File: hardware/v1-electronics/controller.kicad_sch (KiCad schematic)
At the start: 35 parts, among them IC1 IS31FL3733-QFLS4-TR, IC2 IS31FL3733-QFLS4-TR, J2 Conn_01x03, U1 MDBT50Q-1MV2

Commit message: refactor(v1 hardware): power system
Beefed up power system.
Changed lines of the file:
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@@
 		)
 		(fill
-			(type none)
+			(type color)
+			(color 255 229 191 1)
 		)
 	)
@@
 	(rectangle
 		(start 317.5 149.86)
-		(end 381 177.8)
+		(end 368.3 177.8)
 		(stroke
 			(width 0.2)
@@
 	(text "Unassigned Pins"
 		(exclude_from_sim no)
-		(at 370.84 152.4 0)
+		(at 358.14 152.4 0)
 		(effects
 			(font
@@
 		)
 	)
+	(global_label "TPS61288_EN"
+		(shape input)
+		(at 345.44 170.18 0)
+		(fields_autoplaced yes)
+		(effects
+			(font
+				(size 1.27 1.27)
+			)
+			(justify left)
+		)
+		(property "Intersheetrefs" "${INTERSHEET_REFS}"
+			(at 361.3669 170.18 0)
+			(hide yes)
+			(show_name no)
+			(do_not_autoplace no)
+			(effects
+				(font
+					(size 1.27 1.27)
+				)
+				(justify left)
+			)
+		)
+	)
 	(global_label "CS4_2"
 		(shape input)
@@
 	(global_label "BQ25186_INT"
 		(shape input)
-		(at 350.52 160.02 0)
+		(at 345.44 160.02 0)
 		(fields_autoplaced yes)
 		(effects
@@
 		)
 		(property "Intersheetrefs" "${INTERSHEET_REFS}"
-			(at 366.0237 160.02 0)
+			(at 360.9437 160.02 0)
 			(hide yes)
 			(show_name no)
@@
 	(global_label "IS31FL3733_INTB2"
 		(shape input)
-		(at 345.44 165.1 180)
+		(at 340.36 167.64 180)
 		(fields_autoplaced yes)
 		(effects
@@
 		)
 		(property "Intersheetrefs" "${INTERSHEET_REFS}"
-			(at 337.0724 165.1 0)
+			(at 331.9924 167.64 0)
 			(hide yes)
 			(show_name no)
@@
 	(global_label "BQ25186_PG{slash}GPO"
 		(shape input)
-		(at 350.52 162.56 0)
+		(at 345.44 162.56 0)
 		(fields_autoplaced yes)
 		(effects
@@
 		)
 		(property "Intersheetrefs" "${INTERSHEET_REFS}"
-			(at 370.8618 162.56 0)
+			(at 365.7818 162.56 0)
 			(hide yes)
 			(show_name no)
@@
 		)
 	)
+	(global_label "~{MP2721_INT}"
+		(shape input)
+		(at 345.44 172.72 0)
+		(fields_autoplaced yes)
+		(effects
+			(font
+				(size 1.27 1.27)
+			)
+			(justify left)
+		)
+		(property "Intersheetrefs" "${INTERSHEET_REFS}"
+			(at 359.8551 172.72 0)
+			(hide yes)
+			(show_name no)
+			(do_not_autoplace no)
+			(effects
+				(font
+					(size 1.27 1.27)
+				)
+				(justify left)
+			)
+		)
+	)
 	(global_label "RE10_B-Channel"
 		(shape input)
@@
 	(global_label "BQ25186_CE"
 		(shape input)
-		(at 350.52 165.1 0)
+		(at 345.44 165.1 0)
 		(fields_autoplaced yes)
 		(effects
@@
 		)
 		(property "Intersheetrefs" "${INTERSHEET_REFS}"
-			(at 365.5398 165.1 0)
+			(at 360.4598 165.1 0)
 			(hide yes)
 			(show_name no)
@@
 	(global_label "IS31FL3733_INTB1"
 		(shape input)
-		(at 345.44 162.56 180)
+		(at 340.36 165.1 180)
 		(fields_autoplaced yes)
 		(effects
@@
 		)
 		(property "Intersheetrefs" "${INTERSHEET_REFS}"
-			(at 337.0724 162.56 0)
+			(at 331.9924 165.1 0)
 			(hide yes)
 			(show_name no)
@@
 	(global_label "IS31FL3733_SDB2"
 		(shape input)
-		(at 345.44 160.02 180)
+		(at 340.36 162.56 180)
 		(fields_autoplaced yes)
 		(effects
@@
 		)
 		(property "Intersheetrefs" "${INTERSHEET_REFS}"
-			(at 337.4958 160.02 0)
+			(at 332.4158 162.56 0)
 			(hide yes)
 			(show_name no)
@@
 	(global_label "IS31FL3733_SDB1"
 		(shape input)
-		(at 345.44 157.48 180)
+		(at 340.36 160.02 180)
 		(fields_autoplaced yes)
 		(effects
@@
 		)
 		(property "Intersheetrefs" "${INTERSHEET_REFS}"
-			(at 337.4958 157.48 0)
+			(at 332.4158 160.02 0)
 			(hide yes)
 			(show_name no)

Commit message: refactor(v1 hardware): power system refactor complete
- changed components and cleaned up schematic
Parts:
- removed C40: C_Small_US, symbol Device:C_Small_US
- removed C46: C_Small, symbol Device:C_Small
- removed R117, R118: R_Small, symbol Device:R_Small
- added C28: C_Small_US, symbol Device:C_Small_US
- added C40: C_Small, symbol Device:C_Small
- added R104, R105: R_Small, symbol Device:R_Small
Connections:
- net GND: now also C21.2, C23.2, C24.1, R103.1, R113.1, R114.1, R115.1, R116.1, C28.2, C40.1, R105.1; no longer C21.1, C23.1, C24.2, IC1.12 (PGND_2), IC1.5 (PGND_1), IC2.12 (PGND_2), IC2.5 (PGND_1), R103.2, R113.2, R114.2, R116.2
- net IICRST1: now also R113.2; no longer R113.1
- net IICRST2: now also R115.2
- net IS31FL3733_INTB2: now also R104.2; no longer R115.2
- net IS31FL3733_SDB1: now also R103.2; no longer R103.1
- net IS31FL3733_SDB2: now also R105.2; no longer R116.1
- net R_EXT1: now also R114.2; no longer R114.1
- net R_EXT2: now also R116.2
- net VDD: now also C24.2, R104.1; no longer C24.1, R115.1
- net V_SYS: now also C23.1, C28.1, C40.2; no longer C23.2
- net V_RAW_USB renamed VBUS
- net VBUS: now also C21.1; no longer C21.2
- new net Earth: IC1.12 (PGND_2), IC1.5 (PGND_1), IC2.12 (PGND_2), IC2.5 (PGND_1)
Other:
- note added: "High Current Noise Reduction"
- note added: "Not sure about decoupling these"
- note added: "We have 5 open pins. And 6 signals. We could combine interrupts. 4 signals then. and the enables into a single"
- note removed: "I'm uncertain about how to (if at all) decouple the VDD line"
- note removed: "Optional"
- moved on the sheet: C21, C22, C23, C25, C33, C35, C36, C37, C38, C39, J2, R102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

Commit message: feat(v1 hardware): select passives values
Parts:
- removed R43, R44: R_Small, symbol Device:R_Small
- added JP1: Jumper_2_Open, symbol Jumper:Jumper_2_Open
- added SW78: SW_Push, symbol Switch:SW_Push
- C21, C22, C23: value C_Small -> 10μF
- C24, C26, C33, C35, C36, C40, C41, C42: value C_Small -> 0.47μF
- C25, C28: value C_Small_US -> 22μF
- C37, C38, C39, C43, C44, C45: value C_Small -> 0.1μF
- R102, R103, R104, R105, R113, R115: value R_Small -> 100kΩ
- R114, R116: value R_Small -> 13kΩ
- R41, R42: value R_Small -> 10kΩ
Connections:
- net GND: now also SW78.1
- net RESET: now also SW78.2
- net SWDCLK: now also J2.1 (Pin_1)
- net SWDIO: now also J2.3 (Pin_3)
- net SYNC renamed SYNC1
- net SYNC1: now also JP1.1 (A); no longer IC2.40 (SYNC)
- new net SYNC2: IC2.40 (SYNC), JP1.2 (B)
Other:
- note added: "Mention USB here some where"
- note added: "The output current of each current soucecis set to 64mA. Each LED should see about 5mA at max current setting."
- note added: "pick theses based on the capacitance of the line"
- note removed: "USB Config"
- moved on the sheet: J2

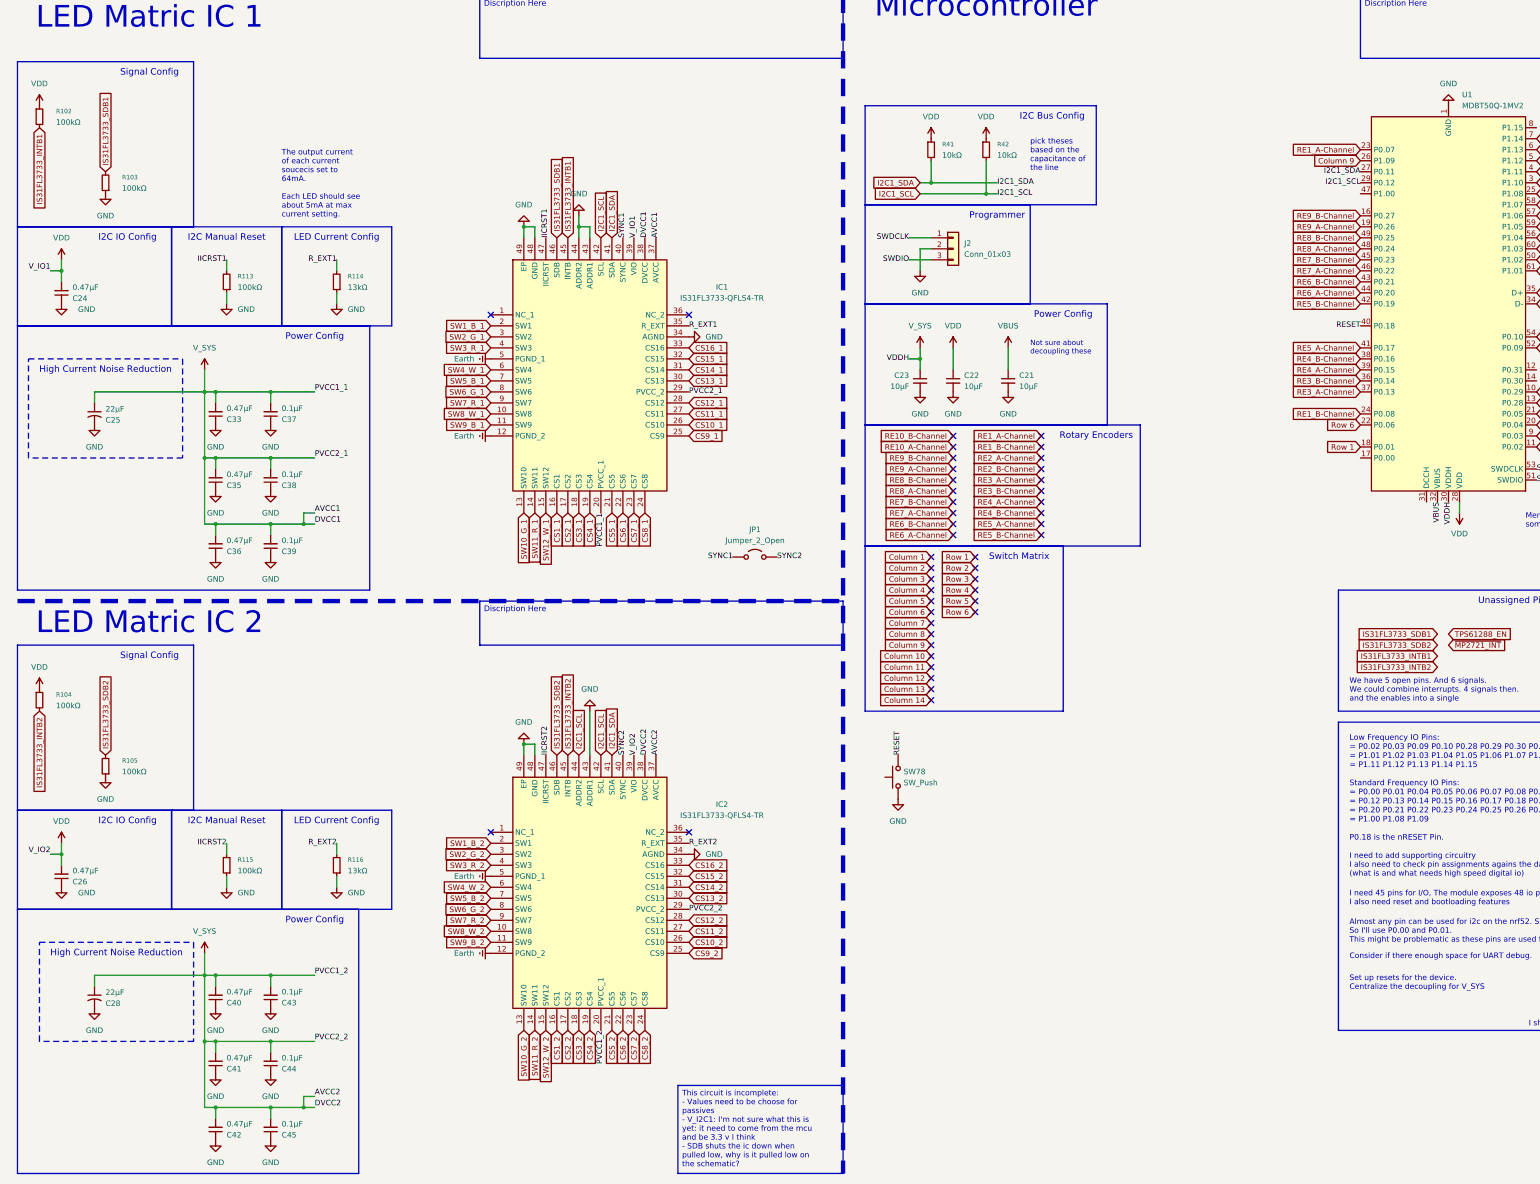
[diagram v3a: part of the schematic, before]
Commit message: refactor(v1 hardware): convert switch matrix to hierarchical pins
made other changes
had claude generate a script for making the convertion
the references for this file still need to be fixed
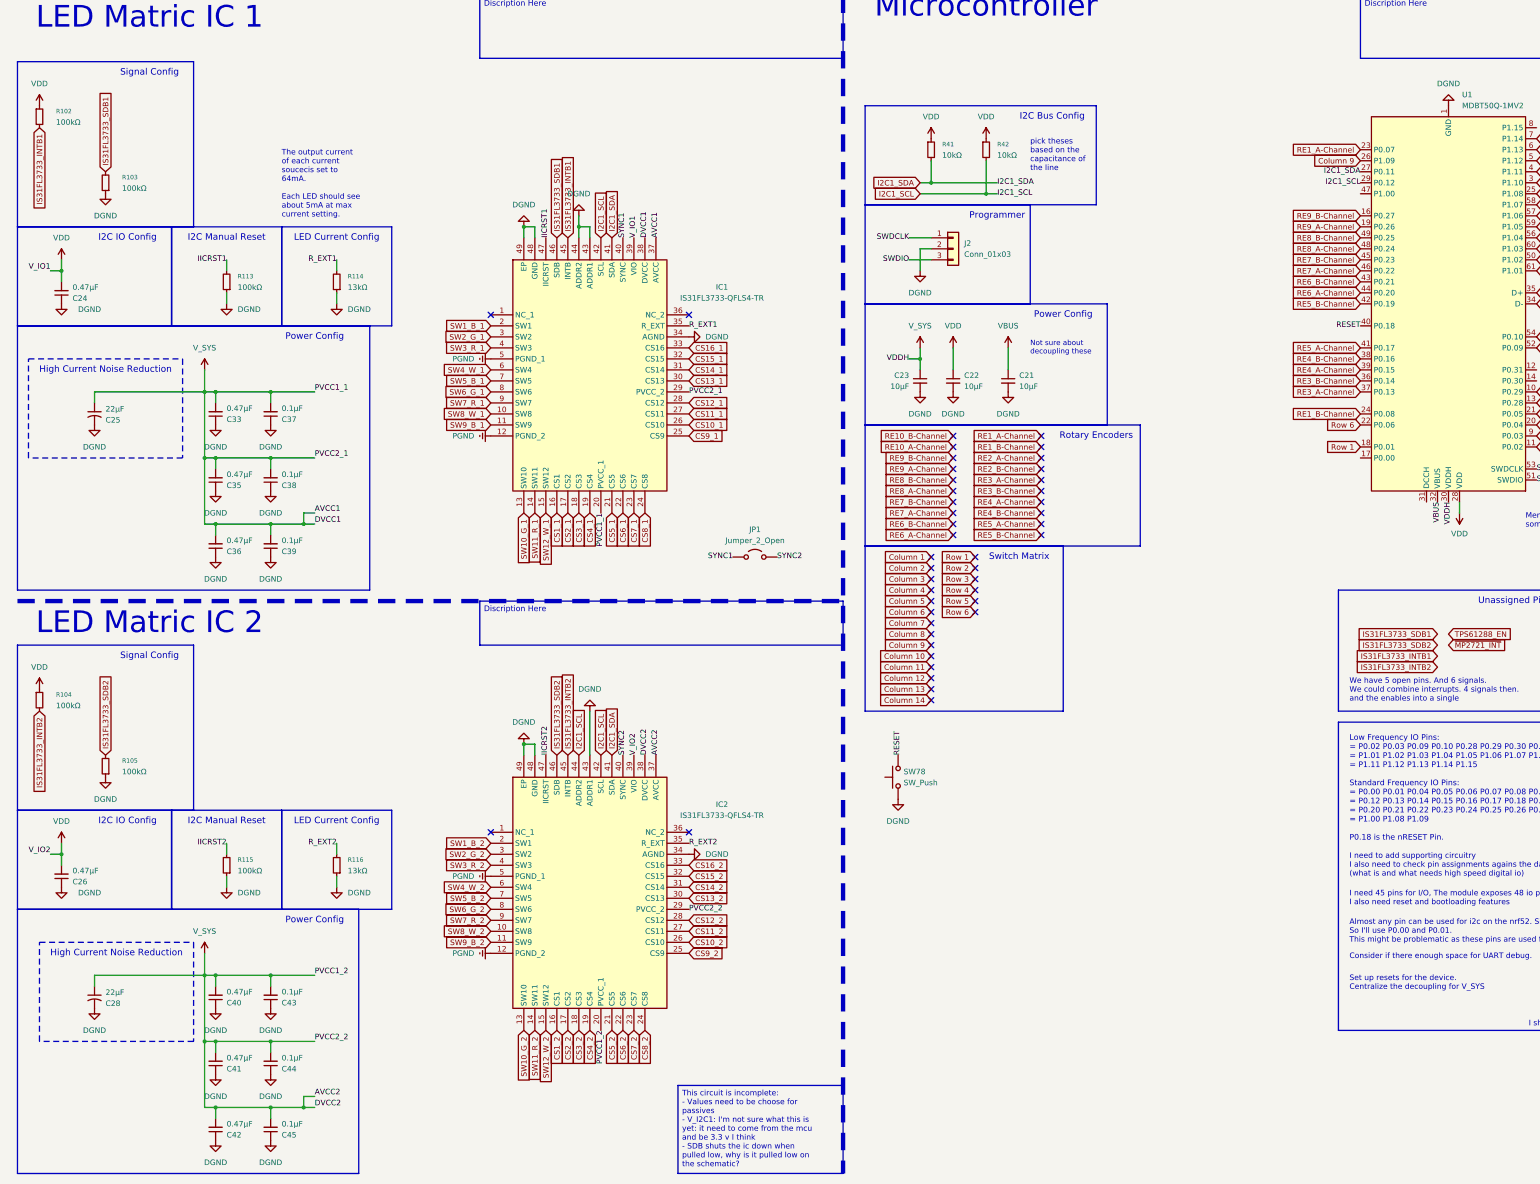
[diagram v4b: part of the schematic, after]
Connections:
- net Earth renamed PGND
- net GND renamed DGND
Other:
- title: (none) -> Slack
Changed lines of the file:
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@@
 	(generator_version "10.0")
 	(paper "A3")
+	(title_block
+		(title "Slack")
+		(date "2026-06-17")
+		(rev "A.0.0")
+	)
 	(rectangle
 		(start 317.5 180.34)
@@
 			)
 		)
-		(property "Value" "GND"
+		(property "Value" "DGND"
 			(at 241.3 109.22 0)
 			(show_name no)
@@
 			)
 		)
-		(property "Value" "GND"
+		(property "Value" "DGND"
 			(at 30.48 251.46 0)
 			(show_name no)
@@
 			)
 		)
-		(property "Value" "GND"
+		(property "Value" "DGND"
 			(at 58.42 251.46 0)
 			(show_name no)
@@
 			)
 		)
-		(property "Value" "GND"
+		(property "Value" "DGND"
 			(at 58.42 147.32 0)
 			(show_name no)
@@
 			)
 		)
-		(property "Value" "GND"
+		(property "Value" "DGND"
 			(at 71.12 251.46 0)
 			(show_name no)
@@
 			)
 		)
-		(property "Value" "GND"
+		(property "Value" "DGND"
 			(at 220.98 81.28 0)
 			(show_name no)
@@
 			)
 		)
-		(property "Value" "GND"
+		(property "Value" "DGND"
 			(at 26.67 85.0899 0)
 			(show_name no)
@@
 			)
 		)
-		(property "Value" "GND"
+		(property "Value" "DGND"
 			(at 144.78 172.72 0)
 			(show_name no)
@@
 			)
 		)
-		(property "Value" "GND"
+		(property "Value" "DGND"
 			(at 71.12 116.84 0)
 			(show_name no)
@@
 			)
 		)
-		(property "Value" "GND"
+		(property "Value" "DGND"
 			(at 71.12 266.7 0)
 			(show_name no)
@@
 			)
 		)
-		(property "Value" "GND"
+		(property "Value" "DGND"
 			(at 71.12 281.94 0)
 			(show_name no)
@@
 			)
 		)
-		(property "Value" "GND"
+		(property "Value" "DGND"
 			(at 88.9 85.0899 0)
 			(show_name no)
@@
 			)
 		)
-		(property "Value" "GND"
+		(property "Value" "DGND"
 			(at 228.6 109.22 0)
 			(show_name no)
@@
 			)
 		)
-		(property "Value" "GND"
+		(property "Value" "DGND"
 			(at 220.98 109.22 0)
 			(show_name no)
@@
 			)
 		)
-		(property "Value" "GND"
+		(property "Value" "DGND"
 			(at 26.67 219.7099 0)
 			(show_name no)
@@
 			)
 		)
-		(property "Value" "GND"
+		(property "Value" "DGND"
 			(at 63.5 219.7099 0)
 			(show_name no)
@@
 			)
 		)
-		(property "Value" "GND"
+		(property "Value" "DGND"
 			(at 88.9 219.7099 0)
 			(show_name no)
@@
 			)
 		)
-		(property "Value" "GND"
+		(property "Value" "DGND"
 			(at 33.02 198.12 0)
 			(show_name no)
@@
 			)
 		)
-		(property "Value" "GND"
+		(property "Value" "DGND"
 			(at 33.02 63.5 0)
 			(show_name no)
@@
 			)
 		)
-		(property "Value" "GND"
+		(property "Value" "DGND"
 			(at 71.12 147.32 0)
 			(show_name no)
@@
 			)
 		)
-		(property "Value" "GND"
+		(property "Value" "DGND"
 			(at 58.42 132.08 0)
 			(show_name no)
@@
 			)
 		)
-		(property "Value" "GND"
+		(property "Value" "DGND"
 			(at 58.42 266.7 0)
 			(show_name no)
@@
 			)
 		)
-		(property "Value" "GND"
+		(property "Value" "DGND"
 			(at 30.48 116.84 0)
 			(show_name no)
@@
 			)
 		)
-		(property "Value" "GND"
+		(property "Value" "DGND"
 			(at 63.5 85.0899 0)
 			(show_name no)
@@
 			)
 		)
-		(property "Value" "Earth"
+		(property "Value" "PGND"
 			(at 118.11 96.5199 90)
 			(show_name no)
@@
 			)
 		)
-		(property "Value" "GND"
+		(property "Value" "DGND"
 			(at 58.42 281.94 0)
 			(show_name no)
@@
 			)
 		)
-		(property "Value" "GND"
+		(property "Value" "DGND"
 			(at 129.54 180.34 0)
 			(show_name no)
@@
 			)
 		)
-		(property "Value" "GND"
+		(property "Value" "DGND"
 			(at 142.24 58.42 0)
 			(show_name no)
@@
 			)
 		)
-		(property "Value" "Earth"
+		(property "Value" "PGND"
 			(at 118.11 114.2999 90)
 			(show_name no)
@@
 			)
 		)
-		(property "Value" "GND"
+		(property "Value" "DGND"
 			(at 71.12 132.08 0)
 			(show_name no)
@@
 			)
 		)
-		(property "Value" "GND"
+		(property "Value" "DGND"
 			(at 171.45 91.4399 90)
 			(show_name no)
@@
 			)
 		)
-		(property "Value" "GND"
+		(property "Value" "DGND"
 			(at 129.54 60.96 0)
 			(show_name no)
@@
 			)
 		)
-		(property "Value" "GND"
+		(property "Value" "DGND"
 			(at 171.45 210.8199 90)
 			(show_name no)
@@
 			)
 		)
-		(property "Value" "GND"
+		(property "Value" "DGND"
 			(at 342.9 33.02 0)
 			(show_name no)
@@
 			)
 		)
-		(property "Value" "Earth"
+		(property "Value" "PGND"
 			(at 118.11 233.6799 90)
 			(show_name no)
@@
 			)
 		)
-		(property "Value" "GND"
+		(property "Value" "DGND"
 			(at 215.9 203.2 0)
 			(show_name no)
@@
 			)
 		)
-		(property "Value" "Earth"
+		(property "Value" "PGND"
 			(at 118.11 215.8999 90)
 			(show_name no)
@@
 			)
 		)
-		(property "Value" "GND"
+		(property "Value" "DGND"
 			(at 58.42 116.84 0)
 			(show_name no)

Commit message: refactor(v1 hardware): all sheets now use hierarchical labels
We'll might change these to buses down the line, but we'll see
I'm happy for now
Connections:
- net VBUS renamed V_BUS
- no-connect marks 44 -> 4
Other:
- note added: "Low Frequency IO Pins: = P0.02 P0.03 P0.09 P0.10 P0.28 P0.29 P0.30 P0.31 = P1.01 P1.02 P1.03 P1.04 P1.05 P1.06 P1.07 P1.10 = P1.11 P1.12 P1.13 P1.14 P1.15 Standard Frequency IO Pins: = P0.00 P0.01 P0.04 P0.05 P0.06 P0.07 P0.08 P0.11 = P0.12 P0.13 P0.14 P0.15 P0.16 P0.17 P0.18 P0.19 = P0.20 P0.21 P0.22 P0.23 P0.24 P0.25 P0.26 P0.27 = P1.00 P1.08 P1.09 P0.18 is the nRESET Pin. Be careful with the p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"
- note removed: "Low Frequency IO Pins: = P0.02 P0.03 P0.09 P0.10 P0.28 P0.29 P0.30 P0.31 = P1.01 P1.02 P1.03 P1.04 P1.05 P1.06 P1.07 P1.10 = P1.11 P1.12 P1.13 P1.14 P1.15 Standard Frequency IO Pins: = P0.00 P0.01 P0.04 P0.05 P0.06 P0.07 P0.08 P0.11 = P0.12 P0.13 P0.14 P0.15 P0.16 P0.17 P0.18 P0.19 = P0.20 P0.21 P0.22 P0.23 P0.24 P0.25 P0.26 P0.27 = P1.00 P1.08 P1.09 P0.18 is the nRESET Pin."
- note removed: "Rotary Encoders"
- note removed: "Switch Matrix"
